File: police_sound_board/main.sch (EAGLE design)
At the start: 16 parts, among them U1 NE555D, U2 NE555D

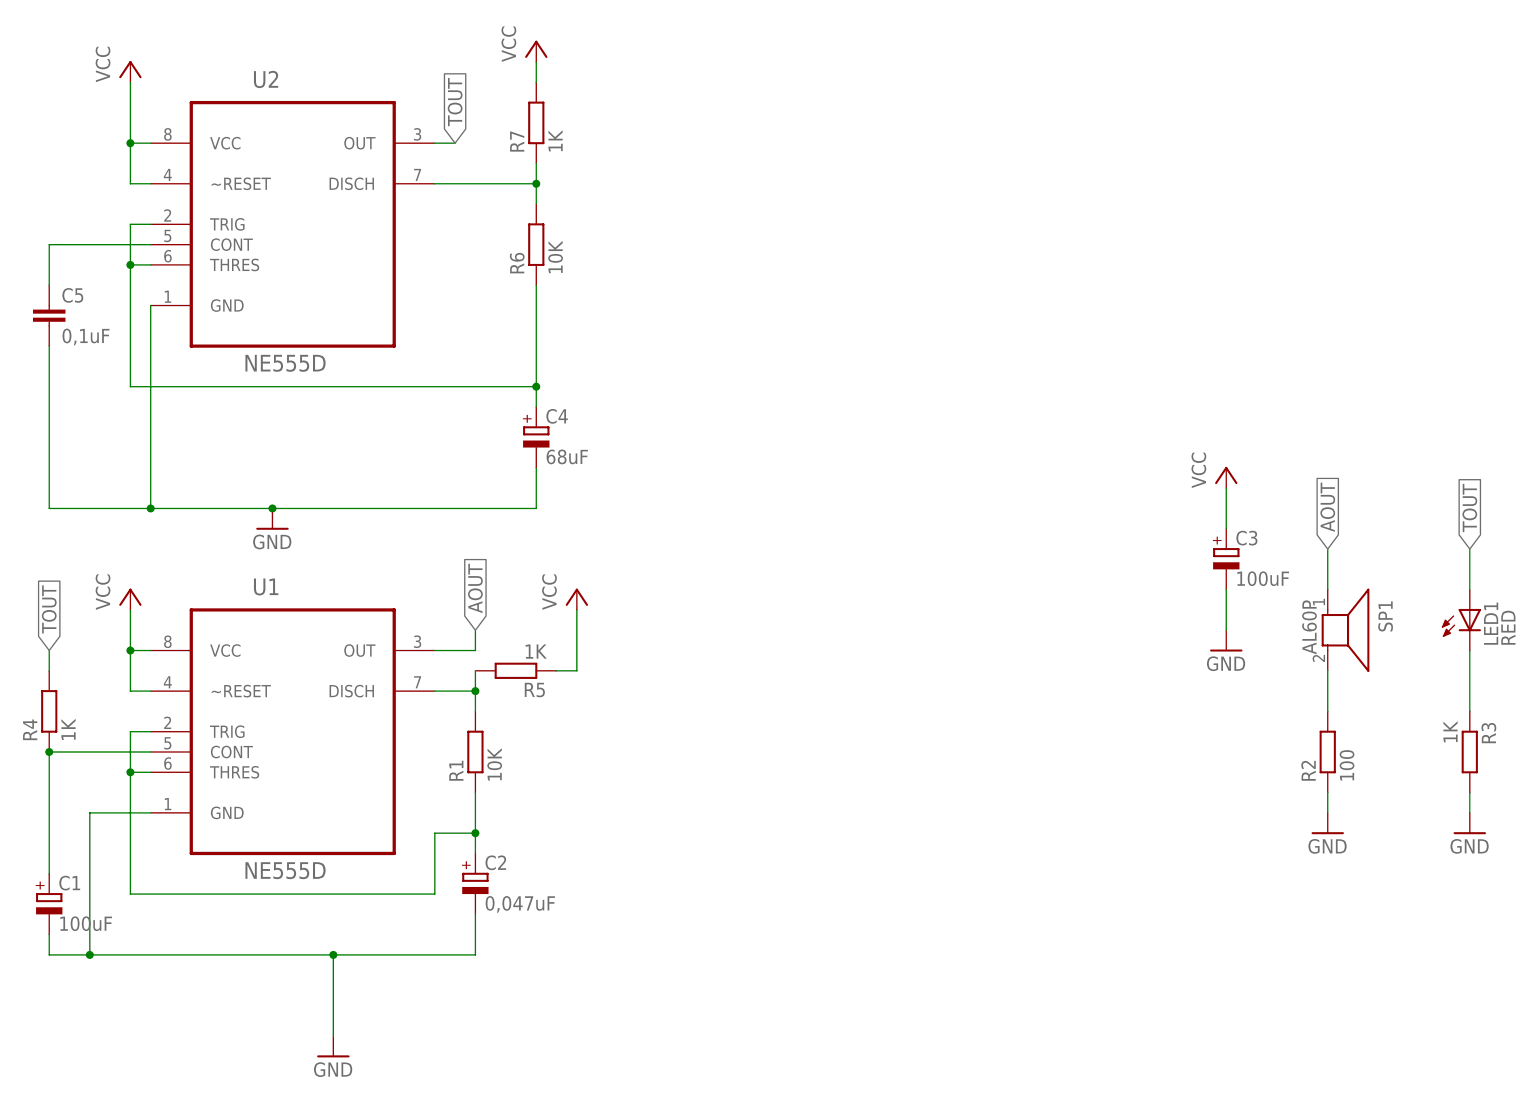
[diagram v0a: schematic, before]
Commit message: removed speaker, added AOUT pin, added power connector pins
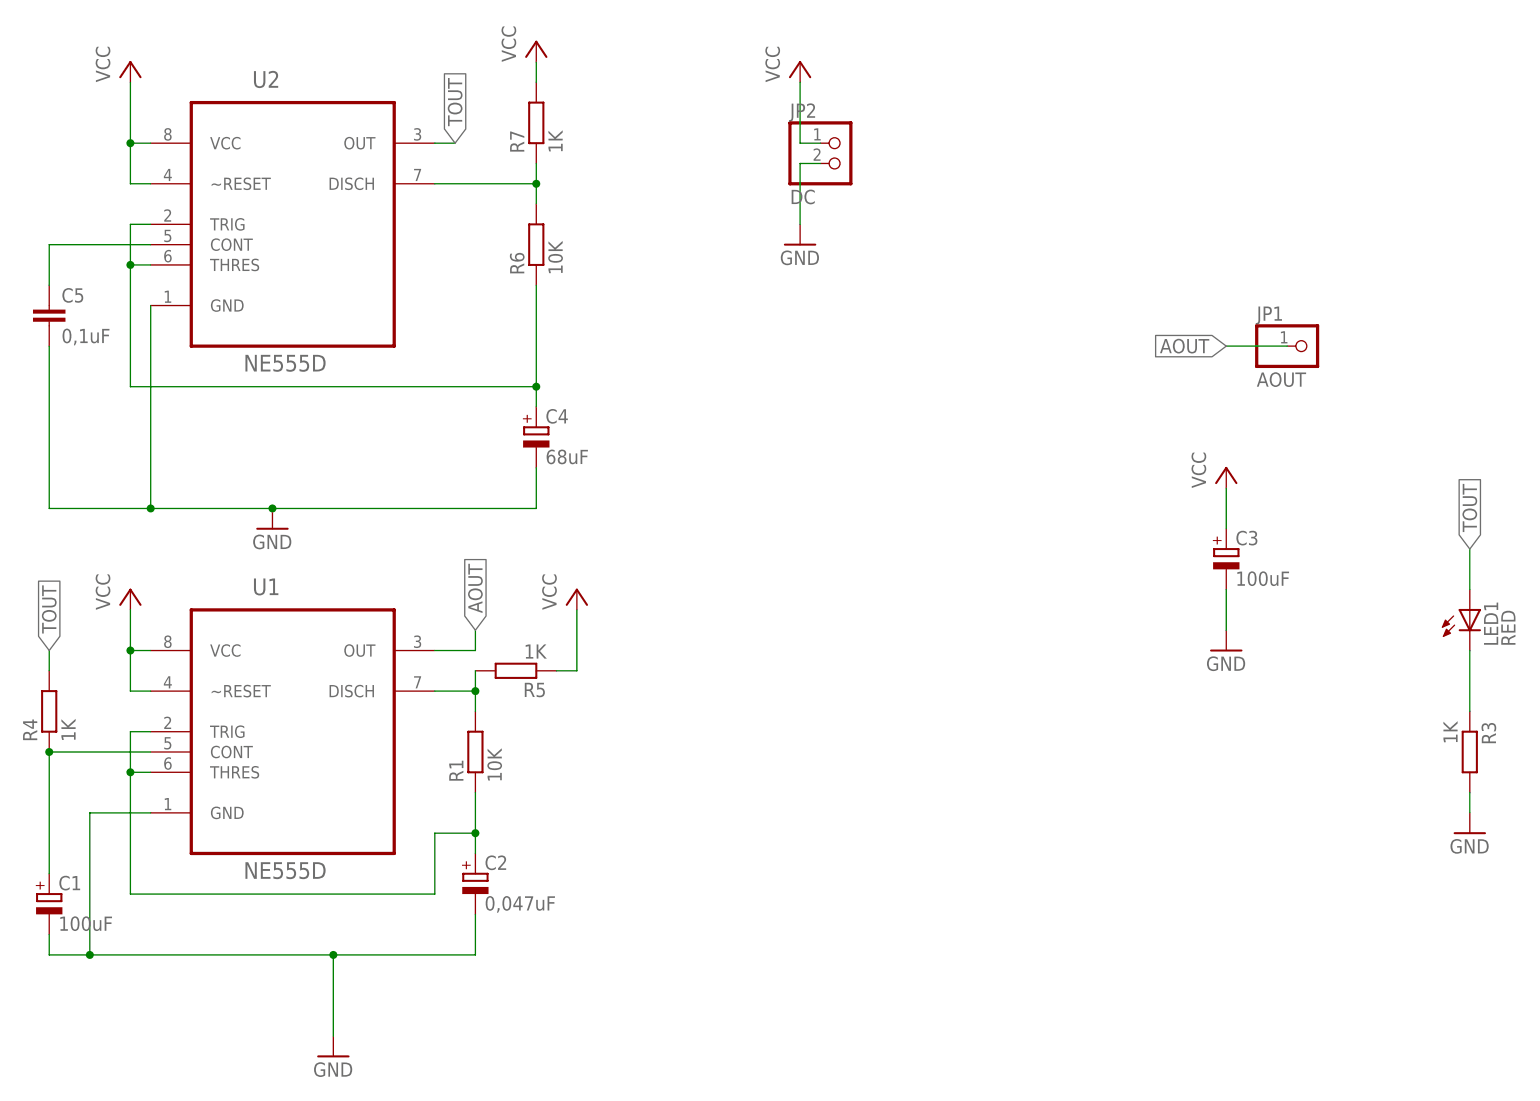
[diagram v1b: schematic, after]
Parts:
- removed R2: 100, resistor:R-EU_0204/7
- removed SP1: AL60P, buzzer:AL60P
- added JP1: AOUT, pinhead:PINHD-1X1
- added JP2: DC, pinhead:PINHD-1X2
- LED1: device led:LED5MM -> led:LEDCHIPLED_0805
- R1, R3, R4, R5, R6, R7: device resistor:R-EU_0204/7 -> resistor:R-EU_R0805
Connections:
- removed net N$1: R2.2, SP1.2
- net AOUT: now also JP1.1; no longer SP1.1
- net GND: now also JP2.2; no longer R2.1
- net VCC: now also JP2.1
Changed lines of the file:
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@@
 <grid distance="0.1" unitdist="inch" unit="inch" style="lines" multiple="1" display="no" altdistance="0.01" altunitdist="inch" altunit="inch"/>
 <layers>
-<layer number="1" name="Top" color="4" fill="1" visible="no" active="no"/>
-<layer number="16" name="Bottom" color="1" fill="1" visible="no" active="no"/>
-<layer number="17" name="Pads" color="2" fill="1" visible="no" active="no"/>
-<layer number="18" name="Vias" color="2" fill="1" visible="no" active="no"/>
-<layer number="19" name="Unrouted" color="6" fill="1" visible="no" active="no"/>
-<layer number="20" name="Dimension" color="15" fill="1" visible="no" active="no"/>
-<layer number="21" name="tPlace" color="7" fill="1" visible="no" active="no"/>
-<layer number="22" name="bPlace" color="7" fill="1" visible="no" active="no"/>
-<layer number="23" name="tOrigins" color="15" fill="1" visible="no" active="no"/>
-<layer number="24" name="bOrigins" color="15" fill="1" visible="no" active="no"/>
-<layer number="25" name="tNames" color="7" fill="1" visible="no" active="no"/>
-<layer number="26" name="bNames" color="7" fill="1" visible="no" active="no"/>
-<layer number="27" name="tValues" color="7" fill="1" visible="no" active="no"/>
-<layer number="28" name="bValues" color="7" fill="1" visible="no" active="no"/>
+<layer number="1" name="Top" color="4" fill="1" visible="yes" active="no"/>
+<layer number="16" name="Bottom" color="1" fill="1" visible="yes" active="no"/>
+<layer number="17" name="Pads" color="2" fill="1" visible="yes" active="no"/>
+<layer number="18" name="Vias" color="2" fill="1" visible="yes" active="no"/>
+<layer number="19" name="Unrouted" color="6" fill="1" visible="yes" active="no"/>
+<layer number="20" name="Dimension" color="15" fill="1" visible="yes" active="no"/>
+<layer number="21" name="tPlace" color="7" fill="1" visible="yes" active="no"/>
+<layer number="22" name="bPlace" color="7" fill="1" visible="yes" active="no"/>
+<layer number="23" name="tOrigins" color="15" fill="1" visible="yes" active="no"/>
+<layer number="24" name="bOrigins" color="15" fill="1" visible="yes" active="no"/>
+<layer number="25" name="tNames" color="7" fill="1" visible="yes" active="no"/>
+<layer number="26" name="bNames" color="7" fill="1" visible="yes" active="no"/>
+<layer number="27" name="tValues" color="7" fill="1" visible="yes" active="no"/>
+<layer number="28" name="bValues" color="7" fill="1" visible="yes" active="no"/>
 <layer number="29" name="tStop" color="7" fill="3" visible="no" active="no"/>
 <layer number="30" name="bStop" color="7" fill="6" visible="no" active="no"/>
@@
 <layer number="35" name="tGlue" color="7" fill="4" visible="no" active="no"/>
 <layer number="36" name="bGlue" color="7" fill="5" visible="no" active="no"/>
-<layer number="37" name="tTest" color="7" fill="1" visible="no" active="no"/>
-<layer number="38" name="bTest" color="7" fill="1" visible="no" active="no"/>
+<layer number="37" name="tTest" color="7" fill="1" visible="yes" active="no"/>
+<layer number="38" name="bTest" color="7" fill="1" visible="yes" active="no"/>
 <layer number="39" name="tKeepout" color="4" fill="11" visible="no" active="no"/>
 <layer number="40" name="bKeepout" color="1" fill="11" visible="no" active="no"/>
@@
 <layer number="44" name="Drills" color="7" fill="1" visible="no" active="no"/>
 <layer number="45" name="Holes" color="7" fill="1" visible="no" active="no"/>
-<layer number="46" name="Milling" color="3" fill="1" visible="no" active="no"/>
-<layer number="47" name="Measures" color="7" fill="1" visible="no" active="no"/>
-<layer number="48" name="Document" color="7" fill="1" visible="no" active="no"/>
-<layer number="49" name="Reference" color="7" fill="1" visible="no" active="no"/>
-<layer number="51" name="tDocu" color="7" fill="1" visible="no" active="no"/>
-<layer number="52" name="bDocu" color="7" fill="1" visible="no" active="no"/>
+<layer number="46" name="Milling" color="3" fill="1" visible="yes" active="no"/>
+<layer number="47" name="Measures" color="7" fill="1" visible="yes" active="no"/>
+<layer number="48" name="Document" color="7" fill="1" visible="yes" active="no"/>
+<layer number="49" name="Reference" color="7" fill="1" visible="yes" active="no"/>
+<layer number="51" name="tDocu" color="7" fill="1" visible="yes" active="no"/>
+<layer number="52" name="bDocu" color="7" fill="1" visible="yes" active="no"/>
 <layer number="90" name="Modules" color="5" fill="1" visible="yes" active="yes"/>
 <layer number="91" name="Nets" color="2" fill="1" visible="yes" active="yes"/>
@@
 <part name="U2" library="Texas Instruments_By_element14_Batch_1" deviceset="NE555D" device=""/>
 <part name="U1" library="Texas Instruments_By_element14_Batch_1" deviceset="NE555D" device=""/>
-<part name="R7" library="resistor" deviceset="R-EU_" device="0204/7" value="1K"/>
-<part name="R6" library="resistor" deviceset="R-EU_" device="0204/7" value="10K"/>
-<part name="R3" library="resistor" deviceset="R-EU_" device="0204/7" value="1K"/>
-<part name="R2" library="resistor" deviceset="R-EU_" device="0204/7" value="100"/>
-<part name="R4" library="resistor" deviceset="R-EU_" device="0204/7" value="1K"/>
-<part name="R1" library="resistor" deviceset="R-EU_" device="0204/7" value="10K"/>
-<part name="R5" library="resistor" deviceset="R-EU_" device="0204/7" value="1K"/>
+<part name="R7" library="resistor" deviceset="R-EU_" device="R0805" value="1K"/>
+<part name="R6" library="resistor" deviceset="R-EU_" device="R0805" value="10K"/>
+<part name="R3" library="resistor" deviceset="R-EU_" device="R0805" value="1K"/>
+<part name="R4" library="resistor" deviceset="R-EU_" device="R0805" value="1K"/>
+<part name="R1" library="resistor" deviceset="R-EU_" device="R0805" value="10K"/>
+<part name="R5" library="resistor" deviceset="R-EU_" device="R0805" value="1K"/>
 <part name="C5" library="resistor" deviceset="C-EU" device="025-025X050" value="0,1uF"/>
 <part name="C3" library="resistor" deviceset="CPOL-EU" device="E3.5-8" value="100uF"/>
@@
 <part name="P+1" library="supply1" deviceset="VCC" device=""/>
 <part name="P+4" library="supply1" deviceset="VCC" device=""/>
-<part name="SP1" library="buzzer" deviceset="AL60P" device=""/>
-<part name="LED1" library="led" deviceset="LED" device="5MM" value="RED"/>
+<part name="LED1" library="led" deviceset="LED" device="CHIPLED_0805" value="RED"/>
 <part name="GND3" library="supply1" deviceset="GND" device=""/>
 <part name="GND4" library="supply1" deviceset="GND" device=""/>
+<part name="JP1" library="pinhead" deviceset="PINHD-1X1" device="" value="AOUT"/>
+<part name="P+6" library="supply1" deviceset="VCC" device=""/>
 <part name="GND2" library="supply1" deviceset="GND" device=""/>
+<part name="JP2" library="pinhead" deviceset="PINHD-1X2" device="" value="DC"/>
 </parts>
 <sheets>
@@
 <instance part="R6" gate="G$1" x="71.12" y="76.2" rot="R90"/>
 <instance part="R3" gate="G$1" x="187.96" y="12.7" rot="R270"/>
-<instance part="R2" gate="G$1" x="170.18" y="12.7" rot="R90"/>
 <instance part="R4" gate="G$1" x="10.16" y="17.78" rot="R90"/>
 <instance part="R1" gate="G$1" x="63.5" y="12.7" rot="R90"/>
@@
 <instance part="P+1" gate="VCC" x="20.32" y="33.02"/>
 <instance part="P+4" gate="VCC" x="20.32" y="99.06"/>
-<instance part="SP1" gate="G$1" x="170.18" y="27.94" rot="R270"/>
 <instance part="LED1" gate="G$1" x="187.96" y="30.48"/>
 <instance part="GND3" gate="1" x="187.96" y="2.54"/>
 <instance part="GND4" gate="1" x="157.48" y="25.4"/>
-<instance part="GND2" gate="1" x="170.18" y="2.54"/>
+<instance part="JP1" gate="G$1" x="167.64" y="63.5"/>
+<instance part="P+6" gate="VCC" x="104.14" y="99.06"/>
+<instance part="GND2" gate="1" x="104.14" y="76.2"/>
+<instance part="JP2" gate="G$1" x="109.22" y="86.36"/>
 </instances>
 <busses>
@@
 <pinref part="R7" gate="G$1" pin="2"/>
 <wire x1="71.12" y1="99.06" x2="71.12" y2="96.52" width="0.1524" layer="91"/>
+</segment>
+<segment>
+<pinref part="P+6" gate="VCC" pin="VCC"/>
+<wire x1="104.14" y1="96.52" x2="104.14" y2="88.9" width="0.1524" layer="91"/>
+<pinref part="JP2" gate="G$1" pin="1"/>
+<wire x1="104.14" y1="88.9" x2="106.68" y2="88.9" width="0.1524" layer="91"/>
 </segment>
 </net>
@@
 </segment>
 <segment>
-<pinref part="R2" gate="G$1" pin="1"/>
-<pinref part="GND2" gate="1" pin="GND"/>
-<wire x1="170.18" y1="7.62" x2="170.18" y2="5.08" width="0.1524" layer="91"/>
-</segment>
-<segment>
 <pinref part="C3" gate="G$1" pin="-"/>
 <pinref part="GND4" gate="1" pin="GND"/>
@@
 <pinref part="GND3" gate="1" pin="GND"/>
 <wire x1="187.96" y1="7.62" x2="187.96" y2="5.08" width="0.1524" layer="91"/>
+</segment>
+<segment>
+<pinref part="JP2" gate="G$1" pin="2"/>
+<pinref part="GND2" gate="1" pin="GND"/>
+<wire x1="106.68" y1="86.36" x2="104.14" y2="86.36" width="0.1524" layer="91"/>
+<wire x1="104.14" y1="86.36" x2="104.14" y2="78.74" width="0.1524" layer="91"/>
 </segment>
 </net>
@@
 </segment>
 <segment>
-<pinref part="SP1" gate="G$1" pin="1"/>
-<wire x1="170.18" y1="33.02" x2="170.18" y2="38.1" width="0.1524" layer="91"/>
-<label x="170.18" y="38.1" size="1.778" layer="95" rot="R90" xref="yes"/>
+<pinref part="JP1" gate="G$1" pin="1"/>
+<wire x1="165.1" y1="63.5" x2="157.48" y2="63.5" width="0.1524" layer="91"/>
+<label x="157.48" y="63.5" size="1.778" layer="95" rot="R180" xref="yes"/>
 </segment>
 </net>
@@
 </segment>
 </net>
-<net name="N$1" class="0">
-<segment>
-<pinref part="SP1" gate="G$1" pin="2"/>
-<pinref part="R2" gate="G$1" pin="2"/>
-<wire x1="170.18" y1="22.86" x2="170.18" y2="17.78" width="0.1524" layer="91"/>
-</segment>
-</net>
